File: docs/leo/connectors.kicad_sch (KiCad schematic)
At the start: 9 parts, among them CN1_A Conn_01x32, CN1_B Conn_01x32, CN1_C Conn_01x32, CN2_A Conn_01x32, CN2_B Conn_01x32, CN2_C Conn_01x32, CN3_A Conn_01x32, CN3_B Conn_01x32

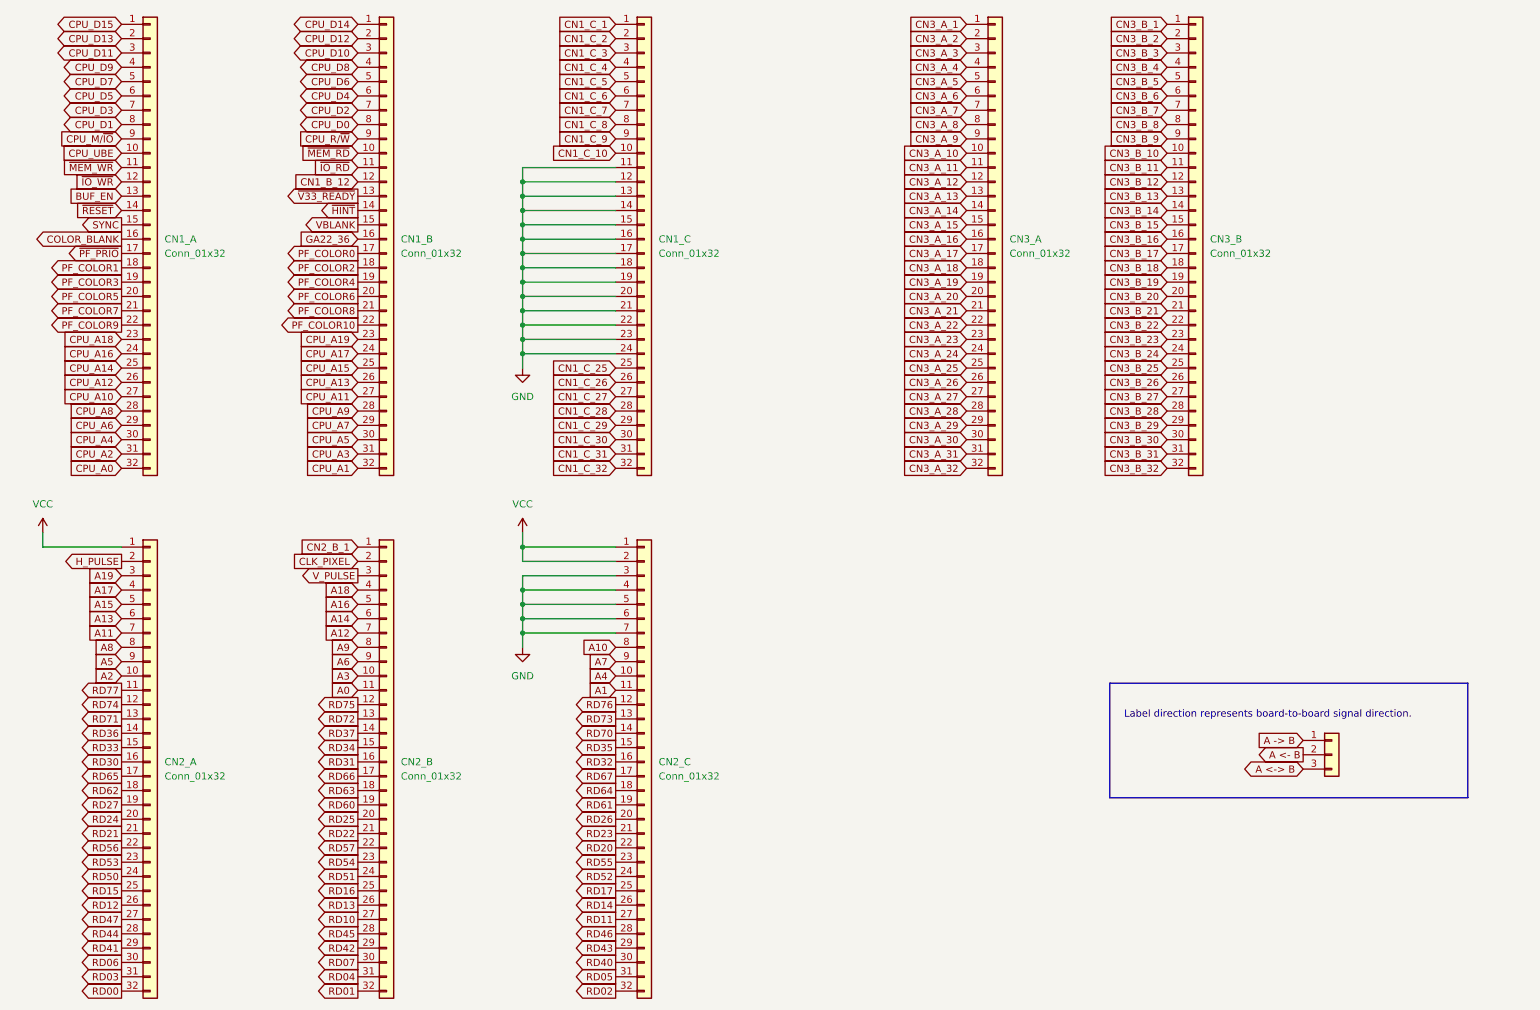
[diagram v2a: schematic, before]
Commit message: Clean up connectors
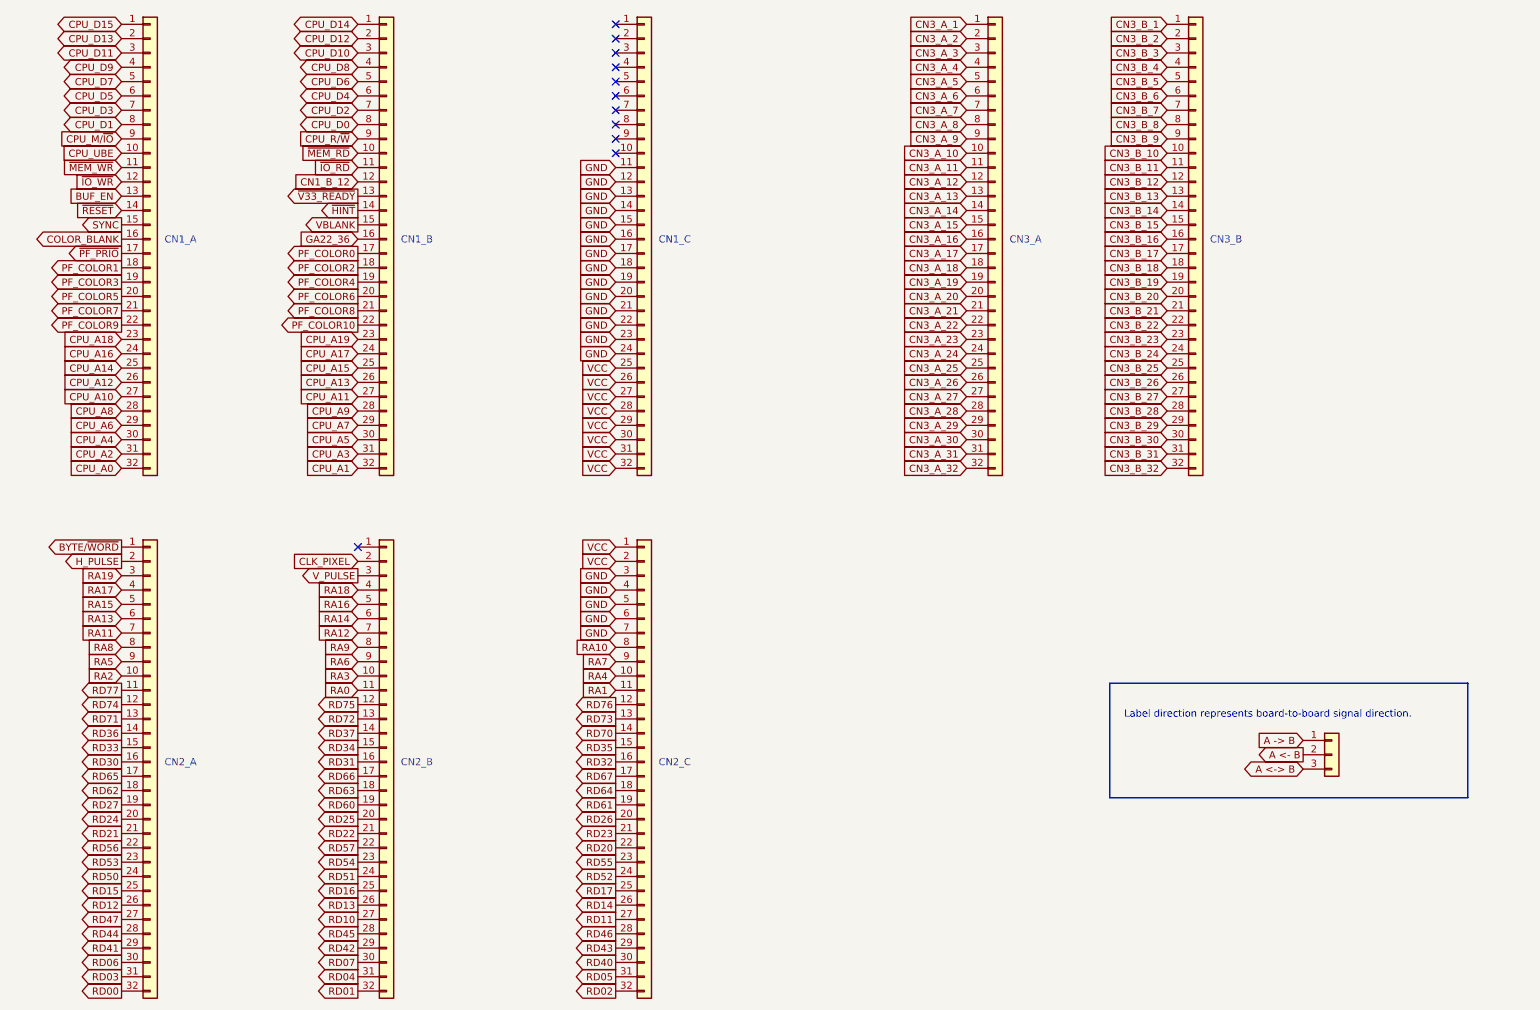
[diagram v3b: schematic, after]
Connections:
- net CN1_C_25 is gone; now on net VCC: CN1_C.25 (Pin_25)
- net CN1_C_26 is gone; now on net VCC: CN1_C.26 (Pin_26)
- net CN1_C_27 is gone; now on net VCC: CN1_C.27 (Pin_27)
- net CN1_C_28 is gone; now on net VCC: CN1_C.28 (Pin_28)
- net CN1_C_29 is gone; now on net VCC: CN1_C.29 (Pin_29)
- net CN1_C_30 is gone; now on net VCC: CN1_C.30 (Pin_30)
- net CN1_C_31 is gone; now on net VCC: CN1_C.31 (Pin_31)
- net CN1_C_32 is gone; now on net VCC: CN1_C.32 (Pin_32)
- net VCC: no longer CN2_A.1 (Pin_1)
- net A0 renamed RA0
- net A1 renamed RA1
- net A10 renamed RA10
- net A11 renamed RA11
- net A12 renamed RA12
- net A13 renamed RA13
- net A14 renamed RA14
- net A15 renamed RA15
- net A16 renamed RA16
- net A17 renamed RA17
- net A18 renamed RA18
- net A19 renamed RA19
- net A2 renamed RA2
- net A3 renamed RA3
- net A4 renamed RA4
- net A5 renamed RA5
- net A6 renamed RA6
- net A7 renamed RA7
- net A8 renamed RA8
- net A9 renamed RA9
- net CN1_C_1: no longer names the net of CN1_C.1 (Pin_1)
- net CN1_C_10: no longer names the net of CN1_C.10 (Pin_10)
- net CN1_C_2: no longer names the net of CN1_C.2 (Pin_2)
- net CN1_C_3: no longer names the net of CN1_C.3 (Pin_3)
- net CN1_C_4: no longer names the net of CN1_C.4 (Pin_4)
- net CN1_C_5: no longer names the net of CN1_C.5 (Pin_5)
- net CN1_C_6: no longer names the net of CN1_C.6 (Pin_6)
- net CN1_C_7: no longer names the net of CN1_C.7 (Pin_7)
- net CN1_C_8: no longer names the net of CN1_C.8 (Pin_8)
- net CN1_C_9: no longer names the net of CN1_C.9 (Pin_9)
- net CN2_B_1: no longer names the net of CN2_B.1 (Pin_1)
- new net BYTE/~{WORD}: CN2_A.1 (Pin_1)
- no-connect marks 0 -> 11

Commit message: Add more b board logic
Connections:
- net BUF_EN renamed ~{LS245_EN}
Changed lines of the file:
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@@
     )
   )
-  (global_label "BUF_EN" (shape input) (at 35.56 49.53 180) (fields_autoplaced)
+  (global_label "~{LS245_EN}" (shape input) (at 35.56 49.53 180) (fields_autoplaced)
     (effects (font (size 1.27 1.27)) (justify right))
     (property "Intersheet References" "${INTERSHEET_REFS}" (id 0) (at 25.1036 49.4506 0)

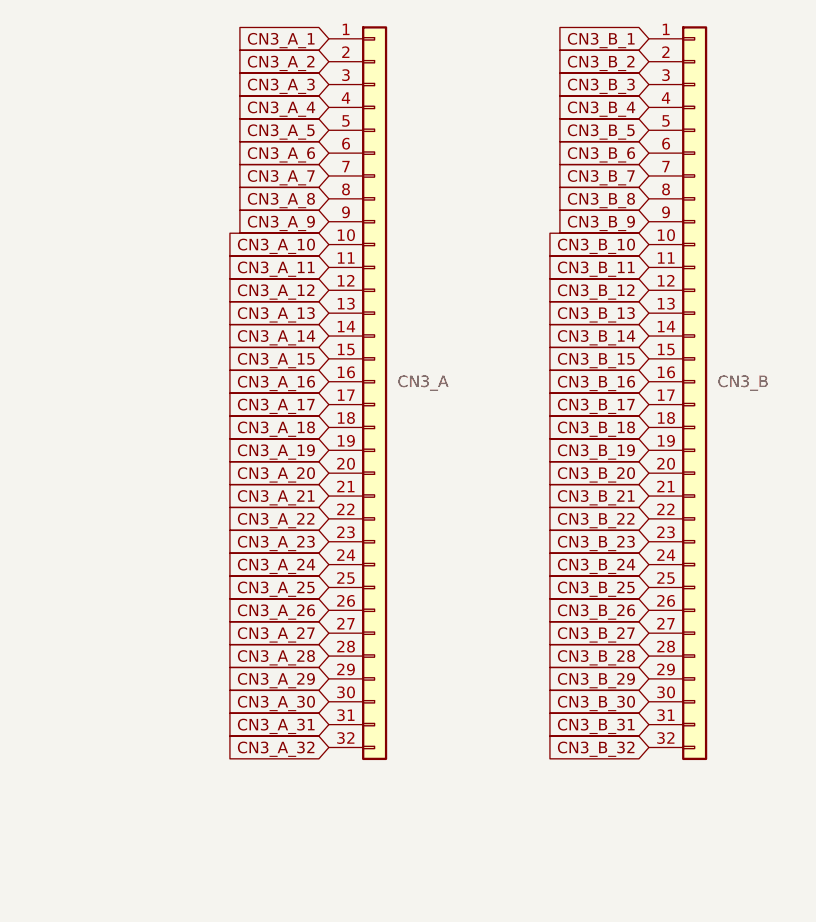
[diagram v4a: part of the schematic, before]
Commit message: B Board Audio section complete
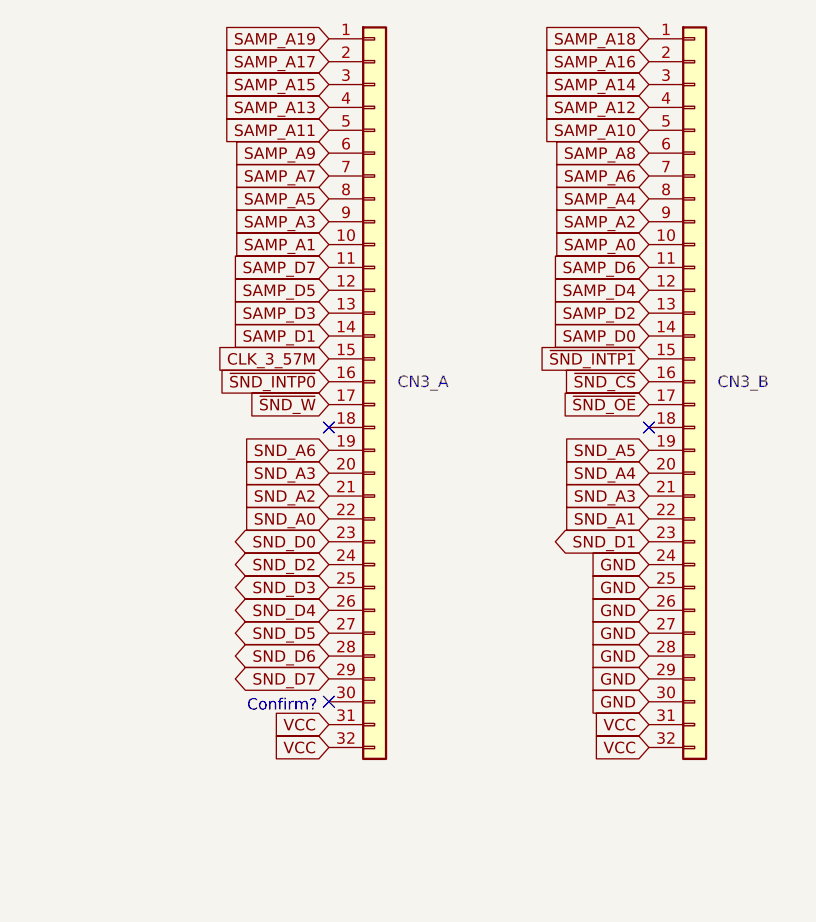
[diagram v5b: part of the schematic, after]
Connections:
- net CN3_A_31 is gone; now on net VCC: CN3_A.31 (Pin_31)
- net CN3_A_32 is gone; now on net VCC: CN3_A.32 (Pin_32)
- net CN3_B_21 is gone; now on net SND_A3: CN3_B.21 (Pin_21)
- net CN3_B_24 is gone; now on net GND: CN3_B.24 (Pin_24)
- net CN3_B_25 is gone; now on net GND: CN3_B.25 (Pin_25)
- net CN3_B_26 is gone; now on net GND: CN3_B.26 (Pin_26)
- net CN3_B_27 is gone; now on net GND: CN3_B.27 (Pin_27)
- net CN3_B_28 is gone; now on net GND: CN3_B.28 (Pin_28)
- net CN3_B_29 is gone; now on net GND: CN3_B.29 (Pin_29)
- net CN3_B_30 is gone; now on net GND: CN3_B.30 (Pin_30)
- net CN3_B_31 is gone; now on net VCC: CN3_B.31 (Pin_31)
- net CN3_B_32 is gone; now on net VCC: CN3_B.32 (Pin_32)
- net CN3_A_1 renamed SAMP_A19
- net CN3_A_10 renamed SAMP_A1
- net CN3_A_11 renamed SAMP_D7
- net CN3_A_12 renamed SAMP_D5
- net CN3_A_13 renamed SAMP_D3
- net CN3_A_14 renamed SAMP_D1
- net CN3_A_15 renamed CLK_3_57M
- net CN3_A_16 renamed ~{SND_INTP0}
- net CN3_A_17 renamed ~{SND_W}
- net CN3_A_18: no longer names the net of CN3_A.18 (Pin_18)
- net CN3_A_19 renamed SND_A6
- net CN3_A_2 renamed SAMP_A17
- net CN3_A_20 renamed SND_A3
- net CN3_A_21 renamed SND_A2
- net CN3_A_22 renamed SND_A0
- net CN3_A_23 renamed SND_D0
- net CN3_A_24 renamed SND_D2
- net CN3_A_25 renamed SND_D3
- net CN3_A_26 renamed SND_D4
- net CN3_A_27 renamed SND_D5
- net CN3_A_28 renamed SND_D6
- net CN3_A_29 renamed SND_D7
- net CN3_A_3 renamed SAMP_A15
- net CN3_A_30: no longer names the net of CN3_A.30 (Pin_30)
- net CN3_A_4 renamed SAMP_A13
- net CN3_A_5 renamed SAMP_A11
- net CN3_A_6 renamed SAMP_A9
- net CN3_A_7 renamed SAMP_A7
- net CN3_A_8 renamed SAMP_A5
- net CN3_A_9 renamed SAMP_A3
- net CN3_B_1 renamed SAMP_A18
- net CN3_B_10 renamed SAMP_A0
- net CN3_B_11 renamed SAMP_D6
- net CN3_B_12 renamed SAMP_D4
- net CN3_B_13 renamed SAMP_D2
- net CN3_B_14 renamed SAMP_D0
- net CN3_B_15 renamed ~{SND_INTP1}
- net CN3_B_16 renamed ~{SND_CS}
- net CN3_B_17 renamed ~{SND_OE}
- net CN3_B_18: no longer names the net of CN3_B.18 (Pin_18)
- net CN3_B_19 renamed SND_A5
- net CN3_B_2 renamed SAMP_A16
- net CN3_B_20 renamed SND_A4
- net CN3_B_22 renamed SND_A1
- net CN3_B_23 renamed SND_D1
- net CN3_B_3 renamed SAMP_A14
- net CN3_B_4 renamed SAMP_A12
- net CN3_B_5 renamed SAMP_A10
- net CN3_B_6 renamed SAMP_A8
- net CN3_B_7 renamed SAMP_A6
- net CN3_B_8 renamed SAMP_A4
- net CN3_B_9 renamed SAMP_A2
- no-connect marks 11 -> 14
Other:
- note added: "Confirm?"

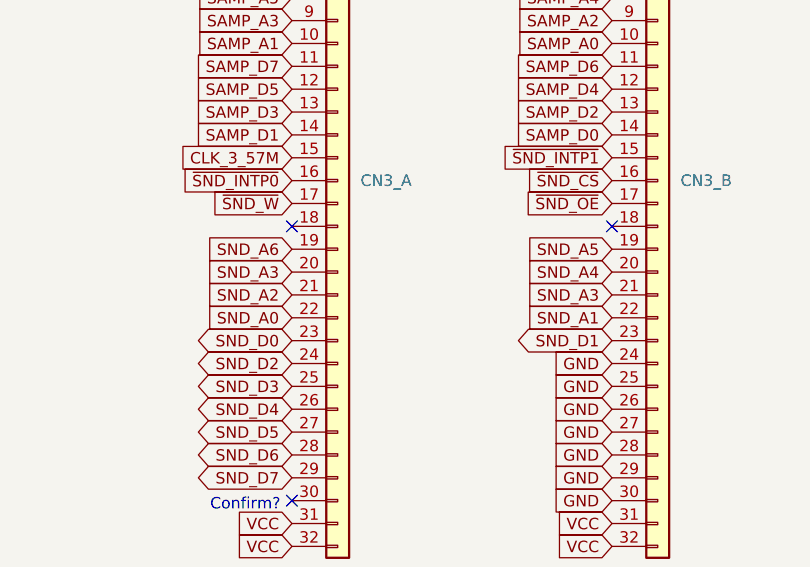
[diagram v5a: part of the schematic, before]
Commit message: Finished GA20 pinout Roughed in sound latch, ym2151 and ga20 signals in A board
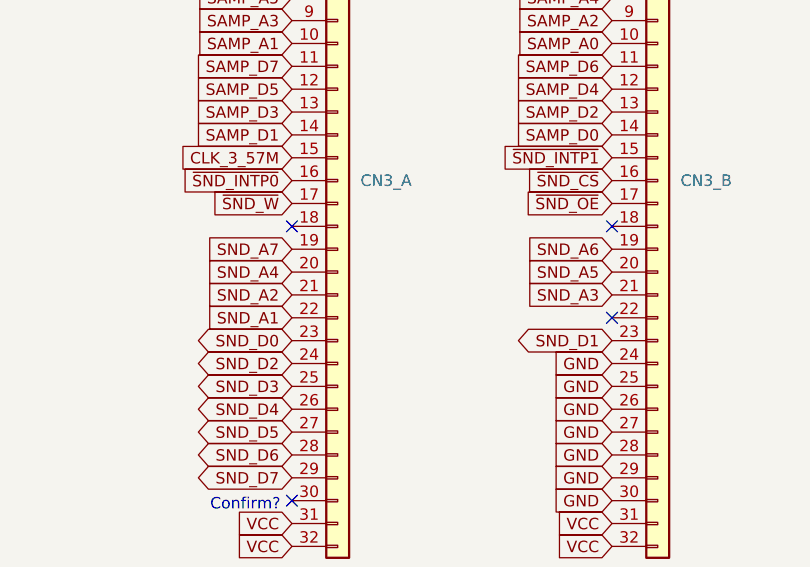
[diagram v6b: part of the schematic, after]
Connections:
- net SND_A0 is gone; now on net SND_A1: CN3_A.22 (Pin_22)
- net SND_A1: no longer CN3_B.22 (Pin_22)
- net SND_A3: no longer CN3_A.20 (Pin_20)
- net SND_A4: now also CN3_A.20 (Pin_20); no longer CN3_B.20 (Pin_20)
- net SND_A5: now also CN3_B.20 (Pin_20); no longer CN3_B.19 (Pin_19)
- net SND_A6: now also CN3_B.19 (Pin_19); no longer CN3_A.19 (Pin_19)
- new net SND_A7: CN3_A.19 (Pin_19)
- no-connect marks 14 -> 15
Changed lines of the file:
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@@
   (no_connect (at 123.19 21.59))
   (no_connect (at 77.47 111.76))
+  (no_connect (at 220.98 72.39))
   (no_connect (at 123.19 29.21))
   (no_connect (at 123.19 31.75))
@@
     )
   )
-  (global_label "SND_A3" (shape input) (at 185.42 67.31 180) (fields_autoplaced)
+  (global_label "SND_A4" (shape input) (at 185.42 67.31 180) (fields_autoplaced)
     (effects (font (size 1.27 1.27)) (justify right))
     (property "Intersheet References" "${INTERSHEET_REFS}" (id 0) (at 175.9312 67.2306 0)
@@
     )
   )
-  (global_label "SND_A5" (shape input) (at 220.98 64.77 180) (fields_autoplaced)
+  (global_label "SND_A6" (shape input) (at 220.98 64.77 180) (fields_autoplaced)
     (effects (font (size 1.27 1.27)) (justify right))
     (property "Intersheet References" "${INTERSHEET_REFS}" (id 0) (at 211.4912 64.6906 0)
@@
     )
   )
-  (global_label "SND_A4" (shape input) (at 220.98 67.31 180) (fields_autoplaced)
+  (global_label "SND_A5" (shape input) (at 220.98 67.31 180) (fields_autoplaced)
     (effects (font (size 1.27 1.27)) (justify right))
     (property "Intersheet References" "${INTERSHEET_REFS}" (id 0) (at 211.4912 67.2306 0)
@@
     )
   )
-  (global_label "SND_A6" (shape input) (at 185.42 64.77 180) (fields_autoplaced)
+  (global_label "SND_A7" (shape input) (at 185.42 64.77 180) (fields_autoplaced)
     (effects (font (size 1.27 1.27)) (justify right))
     (property "Intersheet References" "${INTERSHEET_REFS}" (id 0) (at 175.9312 64.6906 0)
@@
     )
   )
-  (global_label "SND_A1" (shape input) (at 220.98 72.39 180) (fields_autoplaced)
-    (effects (font (size 1.27 1.27)) (justify right))
-    (property "Intersheet References" "${INTERSHEET_REFS}" (id 0) (at 211.4912 72.3106 0)
-      (effects (font (size 1.27 1.27)) (justify right) hide)
-    )
-  )
   (global_label "RD10" (shape output) (at 77.47 177.8 180) (fields_autoplaced)
     (effects (font (size 1.27 1.27)) (justify right))
@@
     )
   )
-  (global_label "SND_A0" (shape input) (at 185.42 72.39 180) (fields_autoplaced)
+  (global_label "SND_A1" (shape input) (at 185.42 72.39 180) (fields_autoplaced)
     (effects (font (size 1.27 1.27)) (justify right))
     (property "Intersheet References" "${INTERSHEET_REFS}" (id 0) (at 175.9312 72.3106 0)

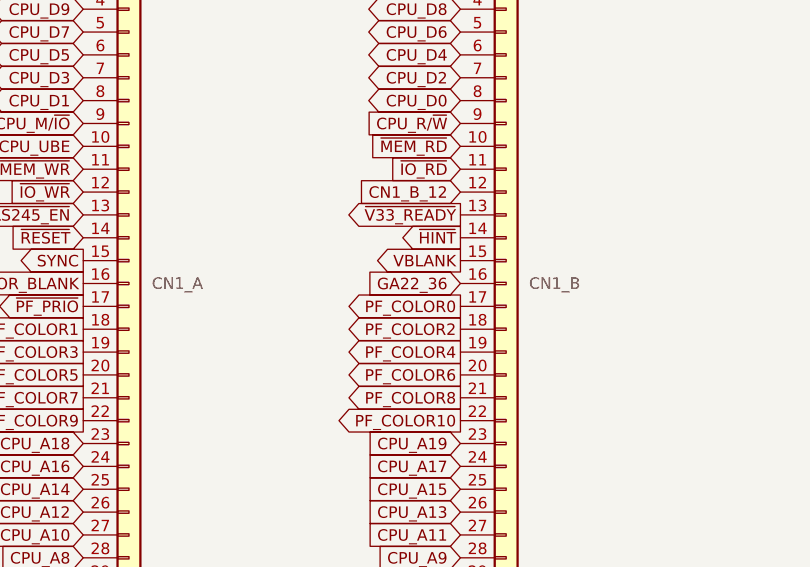
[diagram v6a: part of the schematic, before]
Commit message: Add NL pin Remove unconnected GA23 pins
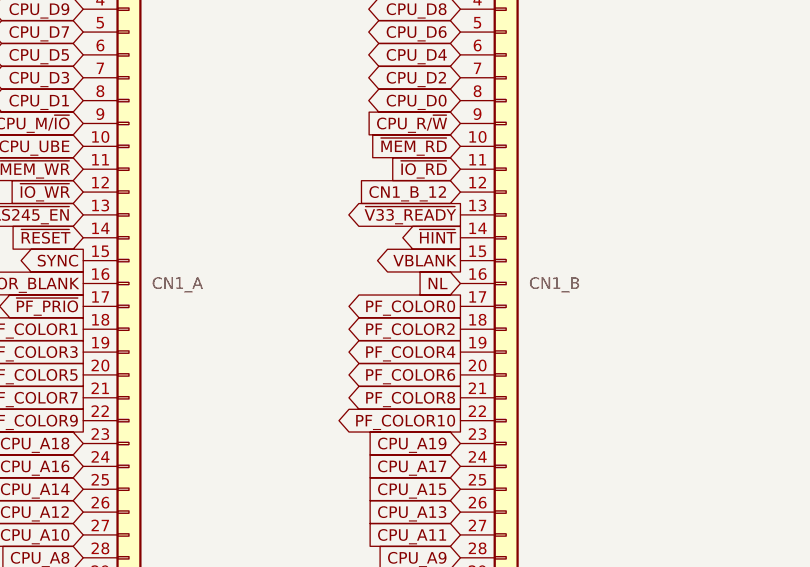
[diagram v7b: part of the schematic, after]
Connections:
- net GA22_36 renamed NL
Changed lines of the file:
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@@
     )
   )
-  (global_label "GA22_36" (shape input) (at 77.47 57.15 180) (fields_autoplaced)
+  (global_label "NL" (shape input) (at 77.47 57.15 180) (fields_autoplaced)
     (effects (font (size 1.27 1.27)) (justify right))
-    (property "Intersheet References" "${INTERSHEET_REFS}" (id 0) (at 66.8321 57.0706 0)
+    (property "Intersheet References" "${INTERSHEET_REFS}" (id 0) (at 72.6983 57.0706 0)
       (effects (font (size 1.27 1.27)) (justify right) hide)
     )
